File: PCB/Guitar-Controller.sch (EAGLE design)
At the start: 34 parts

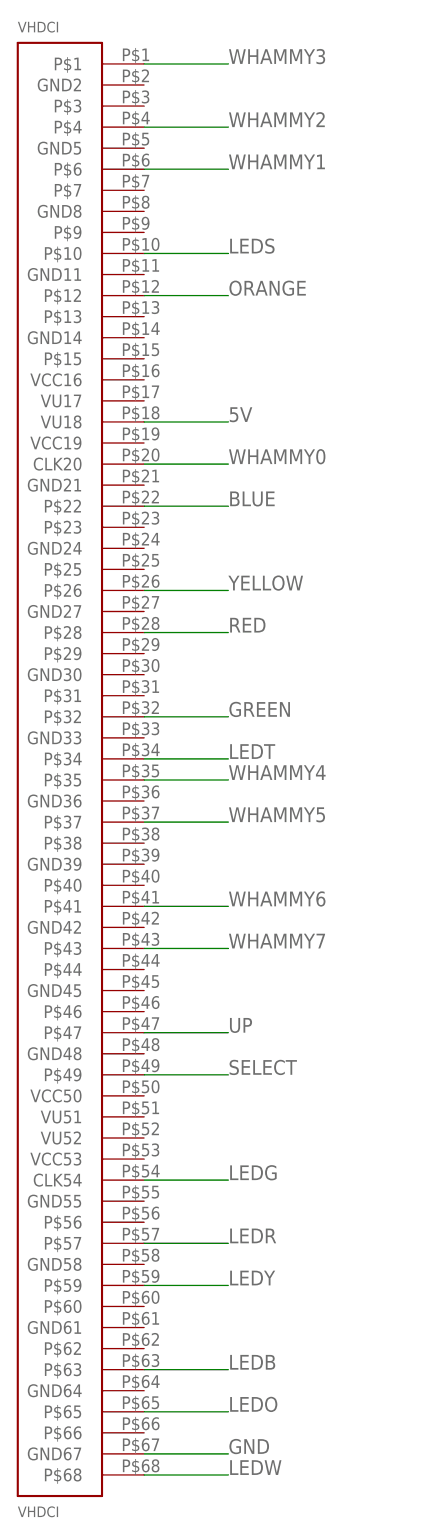
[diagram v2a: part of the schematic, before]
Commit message: PCB: Updated VHDCI connector to match FPGA pins
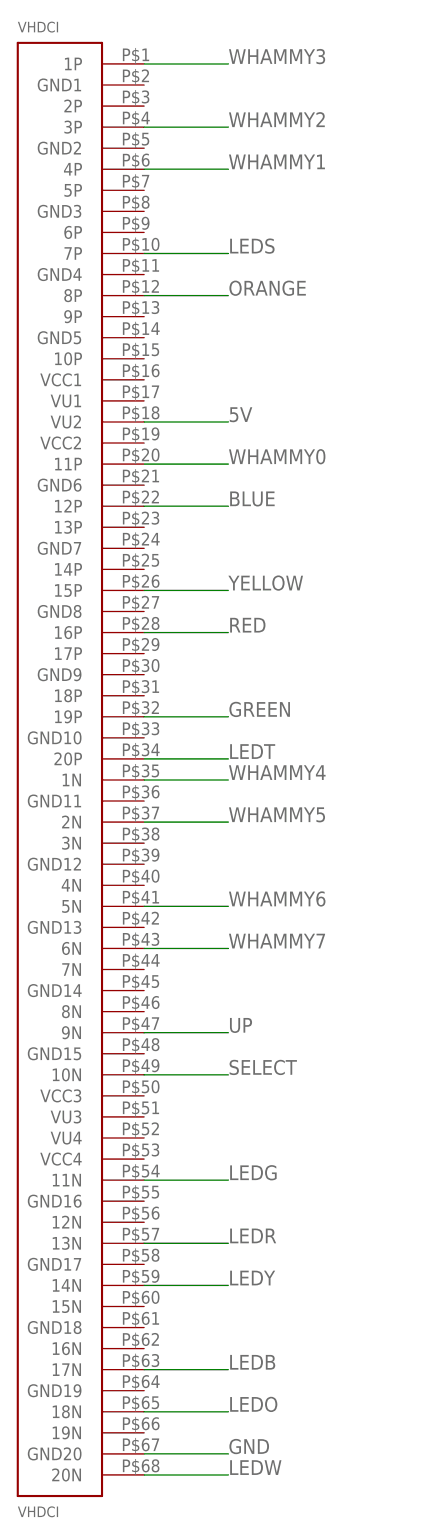
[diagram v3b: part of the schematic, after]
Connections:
- net 5V: now also VHDCI.VU2; no longer VHDCI.VU18
- net BLUE: now also VHDCI.12P; no longer VHDCI.P$22
- net GND: now also VHDCI.GND20; no longer VHDCI.GND67
- net GREEN: now also VHDCI.19P; no longer VHDCI.P$32
- net LEDB: now also VHDCI.17N; no longer VHDCI.P$63
- net LEDG: now also VHDCI.11N; no longer VHDCI.CLK54
- net LEDO: now also VHDCI.18N; no longer VHDCI.P$65
- net LEDR: now also VHDCI.13N; no longer VHDCI.P$57
- net LEDS: now also VHDCI.7P; no longer VHDCI.P$10
- net LEDT: now also VHDCI.20P; no longer VHDCI.P$34
- net LEDW: now also VHDCI.20N; no longer VHDCI.P$68
- net LEDY: now also VHDCI.14N; no longer VHDCI.P$59
- net ORANGE: now also VHDCI.8P; no longer VHDCI.P$12
- net RED: now also VHDCI.16P; no longer VHDCI.P$28
- net SELECT: now also VHDCI.10N; no longer VHDCI.P$49
- net UP: now also VHDCI.9N; no longer VHDCI.P$47
- net WHAMMY0: now also VHDCI.11P; no longer VHDCI.CLK20
- net WHAMMY1: now also VHDCI.4P; no longer VHDCI.P$6
- net WHAMMY2: now also VHDCI.3P; no longer VHDCI.P$4
- net WHAMMY3: now also VHDCI.1P; no longer VHDCI.P$1
- net WHAMMY4: now also VHDCI.1N; no longer VHDCI.P$35
- net WHAMMY5: now also VHDCI.2N; no longer VHDCI.P$37
- net WHAMMY6: now also VHDCI.5N; no longer VHDCI.P$41
- net WHAMMY7: now also VHDCI.6N; no longer VHDCI.P$43
- net YELLOW: now also VHDCI.15P; no longer VHDCI.P$26
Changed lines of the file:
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@@
 <?xml version="1.0" encoding="utf-8"?>
 <!DOCTYPE eagle SYSTEM "eagle.dtd">
-<eagle version="6.3">
+<eagle version="6.4">
 <drawing>
 <settings>
@@
 <setting verticaltext="up"/>
 </settings>
-<grid distance="0.1" unitdist="inch" unit="inch" style="lines" multiple="1" display="yes" altdistance="0.01" altunitdist="inch" altunit="inch"/>
+<grid distance="0.1" unitdist="inch" unit="inch" style="lines" multiple="1" display="no" altdistance="0.01" altunitdist="inch" altunit="inch"/>
 <layers>
 <layer number="1" name="Top" color="4" fill="1" visible="no" active="no"/>
@@
 </segment>
 <segment>
-<pinref part="VHDCI" gate="G$1" pin="GND67"/>
+<pinref part="VHDCI" gate="G$1" pin="GND20"/>
 <wire x1="-40.64" y1="-38.1" x2="-30.48" y2="-38.1" width="0.1524" layer="91"/>
 <label x="-30.48" y="-38.1" size="1.778" layer="95"/>
@@
 </segment>
 <segment>
-<pinref part="VHDCI" gate="G$1" pin="P$1"/>
+<pinref part="VHDCI" gate="G$1" pin="1P"/>
 <wire x1="-30.48" y1="129.54" x2="-40.64" y2="129.54" width="0.1524" layer="91"/>
 <label x="-30.48" y="129.54" size="1.778" layer="95"/>
@@
 </segment>
 <segment>
-<pinref part="VHDCI" gate="G$1" pin="P$35"/>
+<pinref part="VHDCI" gate="G$1" pin="1N"/>
 <wire x1="-30.48" y1="43.18" x2="-40.64" y2="43.18" width="0.1524" layer="91"/>
 <label x="-30.48" y="43.18" size="1.778" layer="95"/>
@@
 </segment>
 <segment>
-<pinref part="VHDCI" gate="G$1" pin="P$37"/>
+<pinref part="VHDCI" gate="G$1" pin="2N"/>
 <wire x1="-30.48" y1="38.1" x2="-40.64" y2="38.1" width="0.1524" layer="91"/>
 <label x="-30.48" y="38.1" size="1.778" layer="95"/>
@@
 </segment>
 <segment>
-<pinref part="VHDCI" gate="G$1" pin="P$28"/>
+<pinref part="VHDCI" gate="G$1" pin="16P"/>
 <wire x1="-30.48" y1="60.96" x2="-40.64" y2="60.96" width="0.1524" layer="91"/>
 <label x="-30.48" y="60.96" size="1.778" layer="95"/>
@@
 </segment>
 <segment>
-<pinref part="VHDCI" gate="G$1" pin="P$26"/>
+<pinref part="VHDCI" gate="G$1" pin="15P"/>
 <wire x1="-30.48" y1="66.04" x2="-40.64" y2="66.04" width="0.1524" layer="91"/>
 <label x="-30.48" y="66.04" size="1.778" layer="95"/>
@@
 </segment>
 <segment>
-<pinref part="VHDCI" gate="G$1" pin="P$12"/>
+<pinref part="VHDCI" gate="G$1" pin="8P"/>
 <wire x1="-30.48" y1="101.6" x2="-40.64" y2="101.6" width="0.1524" layer="91"/>
 <label x="-30.48" y="101.6" size="1.778" layer="95"/>
@@
 </segment>
 <segment>
-<pinref part="VHDCI" gate="G$1" pin="P$47"/>
+<pinref part="VHDCI" gate="G$1" pin="9N"/>
 <wire x1="-30.48" y1="12.7" x2="-40.64" y2="12.7" width="0.1524" layer="91"/>
 <label x="-30.48" y="12.7" size="1.778" layer="95"/>
@@
 </segment>
 <segment>
-<pinref part="VHDCI" gate="G$1" pin="CLK20"/>
+<pinref part="VHDCI" gate="G$1" pin="11P"/>
 <wire x1="-40.64" y1="81.28" x2="-30.48" y2="81.28" width="0.1524" layer="91"/>
 <label x="-30.48" y="81.28" size="1.778" layer="95"/>
@@
 </segment>
 <segment>
-<pinref part="VHDCI" gate="G$1" pin="VU18"/>
+<pinref part="VHDCI" gate="G$1" pin="VU2"/>
 <wire x1="-40.64" y1="86.36" x2="-30.48" y2="86.36" width="0.1524" layer="91"/>
 <label x="-30.48" y="86.36" size="1.778" layer="95"/>
@@
 </segment>
 <segment>
-<pinref part="VHDCI" gate="G$1" pin="P$59"/>
+<pinref part="VHDCI" gate="G$1" pin="14N"/>
 <wire x1="-30.48" y1="-17.78" x2="-40.64" y2="-17.78" width="0.1524" layer="91"/>
 <label x="-30.48" y="-17.78" size="1.778" layer="95"/>
@@
 </segment>
 <segment>
-<pinref part="VHDCI" gate="G$1" pin="P$63"/>
+<pinref part="VHDCI" gate="G$1" pin="17N"/>
 <wire x1="-30.48" y1="-27.94" x2="-40.64" y2="-27.94" width="0.1524" layer="91"/>
 <label x="-30.48" y="-27.94" size="1.778" layer="95"/>
@@
 </segment>
 <segment>
-<pinref part="VHDCI" gate="G$1" pin="P$10"/>
+<pinref part="VHDCI" gate="G$1" pin="7P"/>
 <wire x1="-30.48" y1="106.68" x2="-40.64" y2="106.68" width="0.1524" layer="91"/>
 <label x="-30.48" y="106.68" size="1.778" layer="95"/>
@@
 </segment>
 <segment>
-<pinref part="VHDCI" gate="G$1" pin="P$22"/>
+<pinref part="VHDCI" gate="G$1" pin="12P"/>
 <wire x1="-30.48" y1="76.2" x2="-40.64" y2="76.2" width="0.1524" layer="91"/>
 <label x="-30.48" y="76.2" size="1.778" layer="95"/>
@@
 </segment>
 <segment>
-<pinref part="VHDCI" gate="G$1" pin="P$32"/>
+<pinref part="VHDCI" gate="G$1" pin="19P"/>
 <wire x1="-30.48" y1="50.8" x2="-40.64" y2="50.8" width="0.1524" layer="91"/>
 <label x="-30.48" y="50.8" size="1.778" layer="95"/>
@@
 </segment>
 <segment>
-<pinref part="VHDCI" gate="G$1" pin="P$41"/>
+<pinref part="VHDCI" gate="G$1" pin="5N"/>
 <wire x1="-30.48" y1="27.94" x2="-40.64" y2="27.94" width="0.1524" layer="91"/>
 <label x="-30.48" y="27.94" size="1.778" layer="95"/>
@@
 </segment>
 <segment>
-<pinref part="VHDCI" gate="G$1" pin="P$43"/>
+<pinref part="VHDCI" gate="G$1" pin="6N"/>
 <wire x1="-30.48" y1="22.86" x2="-40.64" y2="22.86" width="0.1524" layer="91"/>
 <label x="-30.48" y="22.86" size="1.778" layer="95"/>
@@
 </segment>
 <segment>
-<pinref part="VHDCI" gate="G$1" pin="P$49"/>
+<pinref part="VHDCI" gate="G$1" pin="10N"/>
 <wire x1="-30.48" y1="7.62" x2="-40.64" y2="7.62" width="0.1524" layer="91"/>
 <label x="-30.48" y="7.62" size="1.778" layer="95"/>
@@
 </segment>
 <segment>
-<pinref part="VHDCI" gate="G$1" pin="CLK54"/>
+<pinref part="VHDCI" gate="G$1" pin="11N"/>
 <wire x1="-40.64" y1="-5.08" x2="-30.48" y2="-5.08" width="0.1524" layer="91"/>
 <label x="-30.48" y="-5.08" size="1.778" layer="95"/>
@@
 </segment>
 <segment>
-<pinref part="VHDCI" gate="G$1" pin="P$57"/>
+<pinref part="VHDCI" gate="G$1" pin="13N"/>
 <wire x1="-30.48" y1="-12.7" x2="-40.64" y2="-12.7" width="0.1524" layer="91"/>
 <label x="-30.48" y="-12.7" size="1.778" layer="95"/>
@@
 </segment>
 <segment>
-<pinref part="VHDCI" gate="G$1" pin="P$34"/>
+<pinref part="VHDCI" gate="G$1" pin="20P"/>
 <wire x1="-30.48" y1="45.72" x2="-40.64" y2="45.72" width="0.1524" layer="91"/>
 <label x="-30.48" y="45.72" size="1.778" layer="95"/>
@@
 </segment>
 <segment>
-<pinref part="VHDCI" gate="G$1" pin="P$65"/>
+<pinref part="VHDCI" gate="G$1" pin="18N"/>
 <wire x1="-30.48" y1="-33.02" x2="-40.64" y2="-33.02" width="0.1524" layer="91"/>
 <label x="-30.48" y="-33.02" size="1.778" layer="95"/>
@@
 </segment>
 <segment>
-<pinref part="VHDCI" gate="G$1" pin="P$68"/>
+<pinref part="VHDCI" gate="G$1" pin="20N"/>
 <wire x1="-30.48" y1="-40.64" x2="-40.64" y2="-40.64" width="0.1524" layer="91"/>
 <label x="-30.48" y="-40.64" size="1.778" layer="95"/>
@@
 </segment>
 <segment>
-<pinref part="VHDCI" gate="G$1" pin="P$6"/>
+<pinref part="VHDCI" gate="G$1" pin="4P"/>
 <wire x1="-30.48" y1="116.84" x2="-40.64" y2="116.84" width="0.1524" layer="91"/>
 <label x="-30.48" y="116.84" size="1.778" layer="95"/>
@@
 </segment>
 <segment>
-<pinref part="VHDCI" gate="G$1" pin="P$4"/>
+<pinref part="VHDCI" gate="G$1" pin="3P"/>
 <wire x1="-30.48" y1="121.92" x2="-40.64" y2="121.92" width="0.1524" layer="91"/>
 <label x="-30.48" y="121.92" size="1.778" layer="95"/>
